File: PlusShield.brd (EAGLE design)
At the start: 82.5 x 67.3 mm, 45 parts, among them K1 G6J-2P-Y, K2 G6J-2P-Y, Q2 SMD, T1 TH

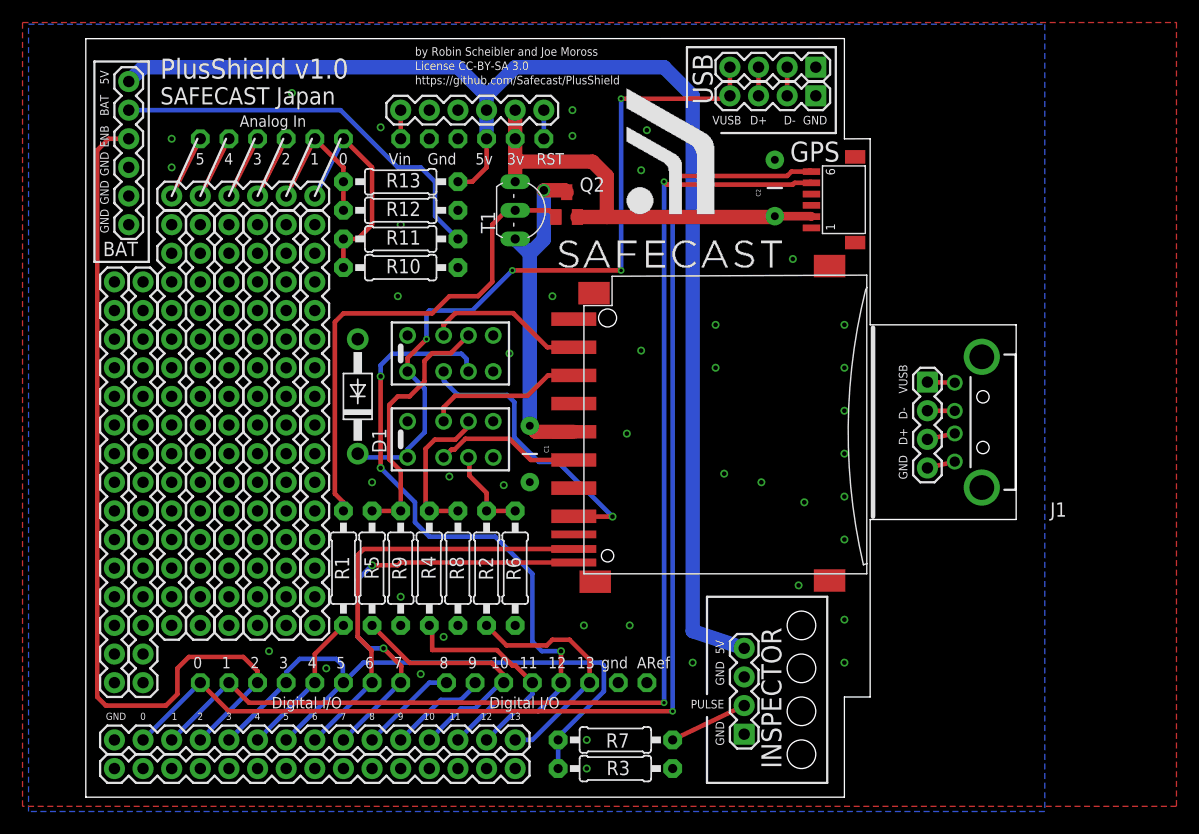
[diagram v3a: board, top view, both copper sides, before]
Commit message: Added switch pins. Moved stuff around. Extra connector for GPS.
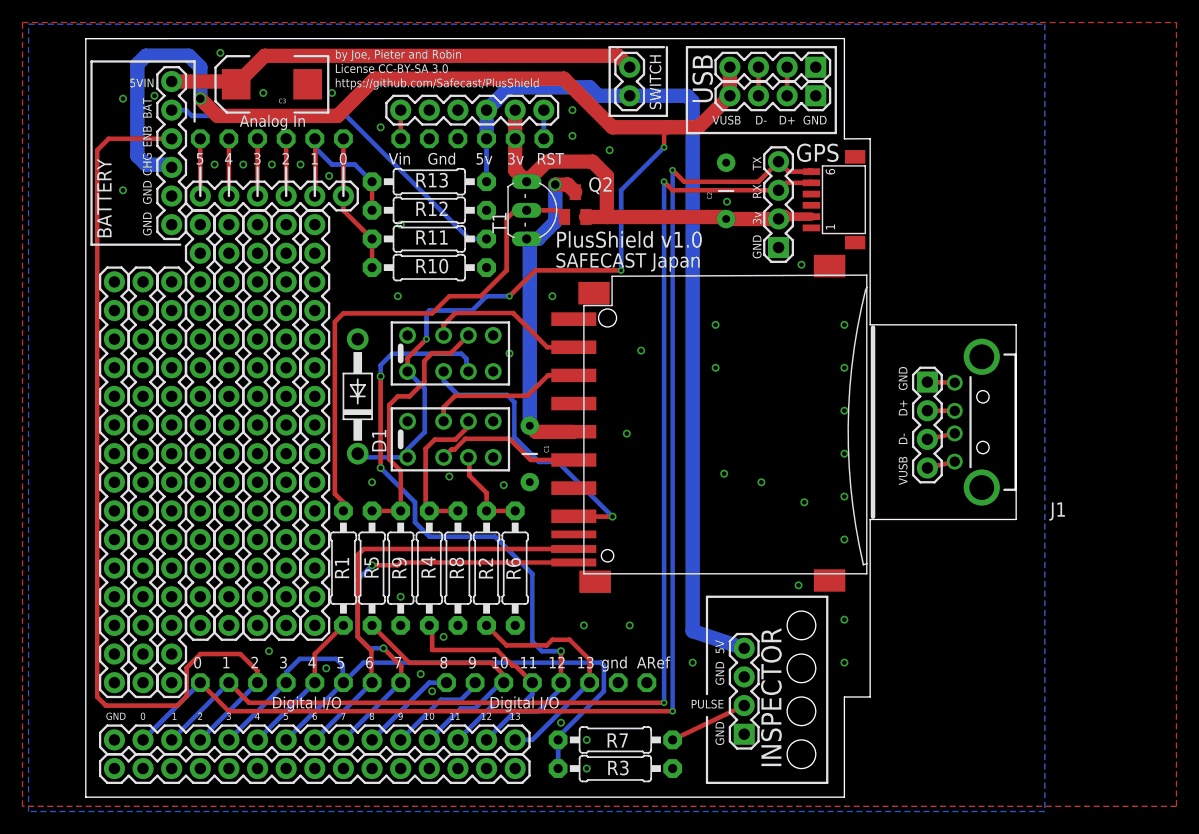
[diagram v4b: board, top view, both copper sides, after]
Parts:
- removed U$5: (no value), Robin:SAFECAST_LOGO
- added C3: 100uF, SparkFun:EIA7343
- added GPS2: (no value), SparkFun:1X04
- added SWI: (no value), SparkFun:1X02
- R2, R4, R5: value 1K -> 10K
- R6, R8, R9: value 1K -> 15K
- moved JP3 5.08 mm to (7.62, 10.2)
- moved C2 4.33 mm to (56.8, 53.8)
- moved JP13 3.81 mm to (7.62, 50.8)
- moved JP9 2.54 mm to (10.2, 53.3)
- moved R10 2.54 mm to (30.5, 47.0)
- moved R11 2.54 mm to (30.5, 49.5)
- moved R12 2.54 mm to (30.5, 52.1)
- moved R13 2.54 mm to (30.5, 54.6)
- moved T1 1.02 mm to (39.1, 52.1)
- moved Q2 0.76 mm to (43.4, 52.6)
- renumbered U$3 to GPS1
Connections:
- removed net N$15: GPS1.6, JP10.2, U$2.D0
- removed net N$16: GPS1.5, JP10.3, U$2.D1
- new net 5VIN: C3.A, JP13.6, SWI.1
- new net RX: GPS1.6, GPS2.4, JP10.2, U$2.D0
- new net TX: GPS1.5, GPS2.3, JP10.3, U$2.D1
- net GND: now also C3.C, GPS2.1, JP13.1; no longer JP13.3
- net VBUS: now also JP13.3
- net VCC3: now also GPS2.2
- net VCC5: now also SWI.2; no longer JP13.6
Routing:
- net RX: track 0.00 -> 112.2 mm, vias 0 -> 2
- net N$15: track 111.0 -> 0.00 mm, vias 2 -> 0
- net TX: track 0.00 -> 106.6 mm, vias 0 -> 2
- net N$16: track 106.1 -> 0.00 mm, vias 2 -> 0
- net VBUS: track 65.7 -> 128.1 mm, vias 4 -> 5
- net 5VIN: track 0.00 -> 42.2 mm
- net VCC5: track 115.5 -> 77.8 mm
- net BATT_SENSE: track 20.0 -> 12.5 mm
- net ENBL: track 78.1 -> 82.3 mm
- net VBATT: track 35.7 -> 32.7 mm
- net VCC5_SENSE: track 13.2 -> 14.8 mm
- net N$24: track 5.68 -> 5.08 mm
- net N$23: track 5.68 -> 5.08 mm
- net N$22: track 5.68 -> 5.08 mm
- net N$21: track 5.68 -> 5.08 mm
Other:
- board text added: "3v"
- board text added: "5VIN"
- board text added: "BATTERY"
- board text added: "CHG"
- board text added: "RX"
- board text added: "SWITCH"
- board text added: "TX"
- board text added: "by Joe, Pieter and Robin"
- board text removed: "by Robin Scheibler and Joe Moross"
